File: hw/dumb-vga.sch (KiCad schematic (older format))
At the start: 21 parts, among them IC1 74HC590N, IC2 74HC590N, IC3 74HC590N, IC4 74HC574N, P1 CONN_01X02, U1 A29040C, X1 VGAF

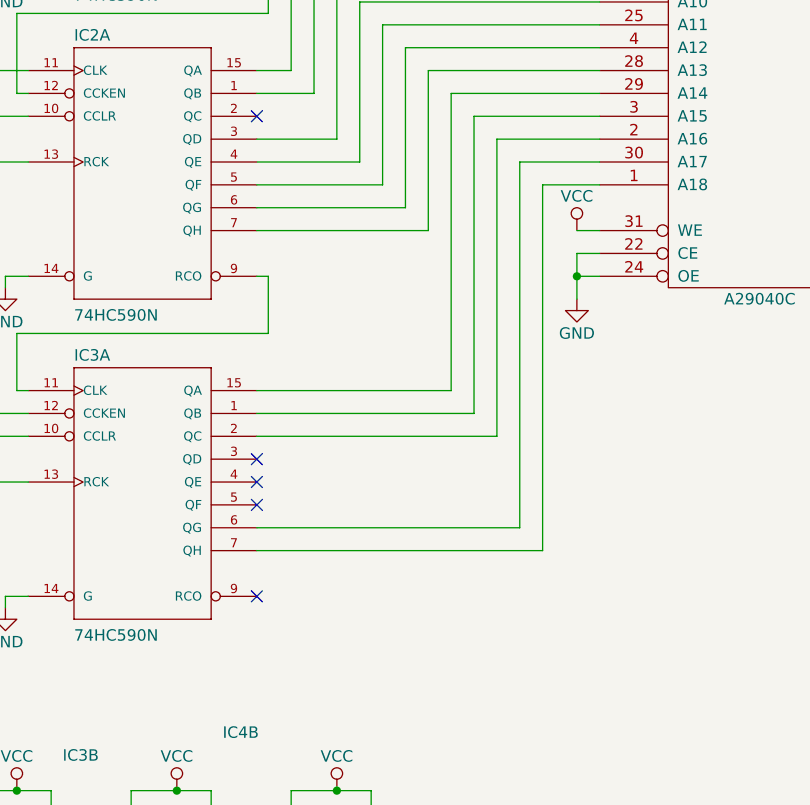
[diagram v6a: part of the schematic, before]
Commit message: Add control over animation rate
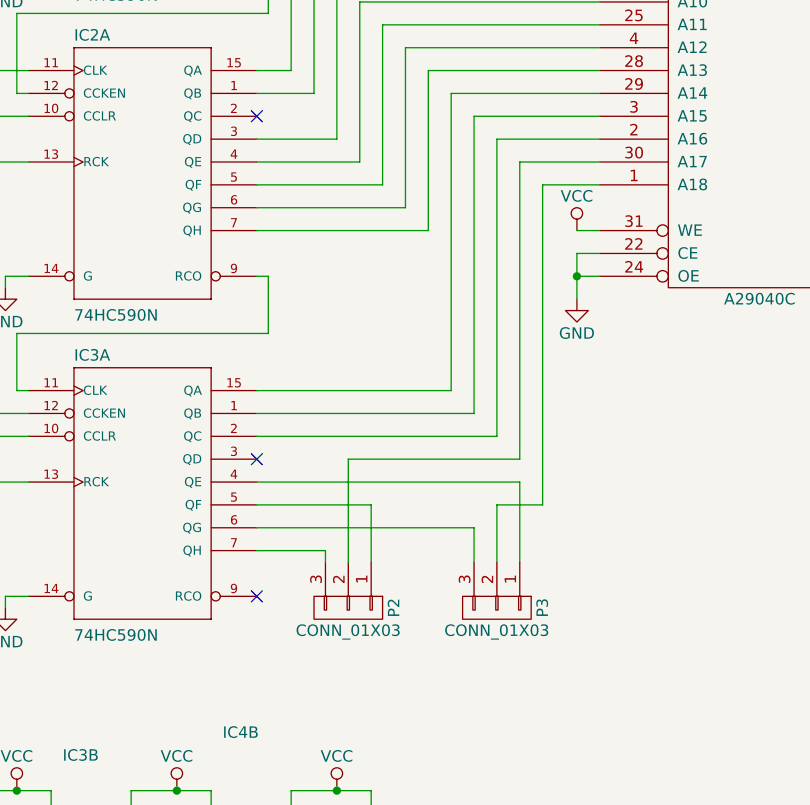
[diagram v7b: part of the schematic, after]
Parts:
- added P2, P3: CONN_01X03, symbol CONN_01X03
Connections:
- net at IC3.4 (QE): now also P3.1 (P1)
- net at IC3.5 (QF): now also P2.1 (P1)
- net at IC3.6 (QG): now also P3.3 (P3); no longer U1.30 (A17)
- net at IC3.7 (QH): now also P2.3 (P3); no longer U1.1 (A18)
- new net: P3.2 (P2), U1.1 (A18)
- new net: P2.2 (P2), U1.30 (A17)
- no-connect marks 14 -> 12
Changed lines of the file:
@@
 Title "Dumb VGA"
 Date ""
-Rev "v0.5"
+Rev "v0.6"
 Comp ""
 Comment1 "Simple circuit to generate VGA-like signal"
@@
 $EndComp
 $Comp
-L VCC #PWR01
+L VCC #PWR11
 U 1 1 56DA1B02
 P 2150 5950
-F 0 "#PWR01" H 2150 5800 50  0001 C CNN
+F 0 "#PWR11" H 2150 5800 50  0001 C CNN
 F 1 "VCC" H 2150 6100 50  0000 C CNN
 F 2 "" H 2150 5950 50  0000 C CNN
@@
 $EndComp
 $Comp
-L VCC #PWR02
+L VCC #PWR21
 U 1 1 56DA1B3E
 P 2850 5950
-F 0 "#PWR02" H 2850 5800 50  0001 C CNN
+F 0 "#PWR21" H 2850 5800 50  0001 C CNN
 F 1 "VCC" H 2850 6100 50  0000 C CNN
 F 2 "" H 2850 5950 50  0000 C CNN
@@
 $EndComp
 $Comp
-L VCC #PWR03
+L VCC #PWR23
 U 1 1 56DA1B5E
 P 3550 5950
-F 0 "#PWR03" H 3550 5800 50  0001 C CNN
+F 0 "#PWR23" H 3550 5800 50  0001 C CNN
 F 1 "VCC" H 3550 6100 50  0000 C CNN
 F 2 "" H 3550 5950 50  0000 C CNN
@@
 $EndComp
 $Comp
-L GND #PWR04
+L GND #PWR24
 U 1 1 56DA1EF3
 P 3550 6750
-F 0 "#PWR04" H 3550 6500 50  0001 C CNN
+F 0 "#PWR24" H 3550 6500 50  0001 C CNN
 F 1 "GND" H 3550 6600 50  0000 C CNN
 F 2 "" H 3550 6750 50  0000 C CNN
@@
 $EndComp
 $Comp
-L GND #PWR05
+L GND #PWR22
 U 1 1 56DA1FE2
 P 2850 6750
-F 0 "#PWR05" H 2850 6500 50  0001 C CNN
+F 0 "#PWR22" H 2850 6500 50  0001 C CNN
 F 1 "GND" H 2850 6600 50  0000 C CNN
 F 2 "" H 2850 6750 50  0000 C CNN
@@
 $EndComp
 $Comp
-L GND #PWR06
+L GND #PWR12
 U 1 1 56DA2011
 P 2150 6750
-F 0 "#PWR06" H 2150 6500 50  0001 C CNN
+F 0 "#PWR12" H 2150 6500 50  0001 C CNN
 F 1 "GND" H 2150 6600 50  0000 C CNN
 F 2 "" H 2150 6750 50  0000 C CNN
@@
 $EndComp
 NoConn ~ 3900 5100
-NoConn ~ 3900 4500
-NoConn ~ 3900 4600
-NoConn ~ 3900 4700
 $Comp
 L XO-8 QG1
@@
 $EndComp
 $Comp
-L VCC #PWR07
+L VCC #PWR3
 U 1 1 56DA29D7
 P 950 1100
-F 0 "#PWR07" H 950 950 50  0001 C CNN
+F 0 "#PWR3" H 950 950 50  0001 C CNN
 F 1 "VCC" H 950 1250 50  0000 C CNN
 F 2 "" H 950 1100 50  0000 C CNN
@@
 $EndComp
 $Comp
-L GND #PWR08
+L GND #PWR4
 U 1 1 56DA2A09
 P 950 1700
-F 0 "#PWR08" H 950 1450 50  0001 C CNN
+F 0 "#PWR4" H 950 1450 50  0001 C CNN
 F 1 "GND" H 950 1550 50  0000 C CNN
 F 2 "" H 950 1700 50  0000 C CNN
@@
 NoConn ~ 2050 1200
 $Comp
-L GND #PWR09
+L GND #PWR28
 U 1 1 56DA2E52
 P 5300 3800
-F 0 "#PWR09" H 5300 3550 50  0001 C CNN
+F 0 "#PWR28" H 5300 3550 50  0001 C CNN
 F 1 "GND" H 5300 3650 50  0000 C CNN
 F 2 "" H 5300 3800 50  0000 C CNN
@@
 $EndComp
 $Comp
-L VCC #PWR010
+L VCC #PWR27
 U 1 1 56DA2FBD
 P 5300 3500
-F 0 "#PWR010" H 5300 3350 50  0001 C CNN
+F 0 "#PWR27" H 5300 3350 50  0001 C CNN
 F 1 "VCC" H 5300 3650 50  0000 C CNN
 F 2 "" H 5300 3500 50  0000 C CNN
@@
 $EndComp
 $Comp
-L GND #PWR011
+L GND #PWR18
 U 1 1 56DA30CB
 P 2800 2350
-F 0 "#PWR011" H 2800 2100 50  0001 C CNN
+F 0 "#PWR18" H 2800 2100 50  0001 C CNN
 F 1 "GND" H 2800 2200 50  0000 C CNN
 F 2 "" H 2800 2350 50  0000 C CNN
@@
 $EndComp
 $Comp
-L GND #PWR012
+L GND #PWR19
 U 1 1 56DA30FD
 P 2800 3750
-F 0 "#PWR012" H 2800 3500 50  0001 C CNN
+F 0 "#PWR19" H 2800 3500 50  0001 C CNN
 F 1 "GND" H 2800 3600 50  0000 C CNN
 F 2 "" H 2800 3750 50  0000 C CNN
@@
 $EndComp
 $Comp
-L GND #PWR013
+L GND #PWR20
 U 1 1 56DA31B1
 P 2800 5150
-F 0 "#PWR013" H 2800 4900 50  0001 C CNN
+F 0 "#PWR20" H 2800 4900 50  0001 C CNN
 F 1 "GND" H 2800 5000 50  0000 C CNN
 F 2 "" H 2800 5150 50  0000 C CNN
@@
 $EndComp
 $Comp
-L GND #PWR014
+L GND #PWR16
 U 1 1 56DA3E4A
 P 2500 1700
-F 0 "#PWR014" H 2500 1450 50  0001 C CNN
+F 0 "#PWR16" H 2500 1450 50  0001 C CNN
 F 1 "GND" H 2500 1550 50  0000 C CNN
 F 2 "" H 2500 1700 50  0000 C CNN
@@
 $EndComp
 $Comp
-L GND #PWR015
+L GND #PWR17
 U 1 1 56DA3EAE
 P 2500 4500
-F 0 "#PWR015" H 2500 4250 50  0001 C CNN
+F 0 "#PWR17" H 2500 4250 50  0001 C CNN
 F 1 "GND" H 2500 4350 50  0000 C CNN
 F 2 "" H 2500 4500 50  0000 C CNN
@@
 $EndComp
 $Comp
-L VCC #PWR016
+L VCC #PWR13
 U 1 1 56DA4042
 P 2350 1600
-F 0 "#PWR016" H 2350 1450 50  0001 C CNN
+F 0 "#PWR13" H 2350 1450 50  0001 C CNN
 F 1 "VCC" H 2350 1750 50  0000 C CNN
 F 2 "" H 2350 1600 50  0000 C CNN
@@
 $EndComp
 $Comp
-L VCC #PWR017
+L VCC #PWR14
 U 1 1 56DA4074
 P 2350 3000
-F 0 "#PWR017" H 2350 2850 50  0001 C CNN
+F 0 "#PWR14" H 2350 2850 50  0001 C CNN
 F 1 "VCC" H 2350 3150 50  0000 C CNN
 F 2 "" H 2350 3000 50  0000 C CNN
@@
 $EndComp
 $Comp
-L VCC #PWR018
+L VCC #PWR15
 U 1 1 56DA40E7
 P 2350 4400
-F 0 "#PWR018" H 2350 4250 50  0001 C CNN
+F 0 "#PWR15" H 2350 4250 50  0001 C CNN
 F 1 "VCC" H 2350 4550 50  0000 C CNN
 F 2 "" H 2350 4400 50  0000 C CNN
@@
 $EndComp
 $Comp
-L VCC #PWR019
+L VCC #PWR9
 U 1 1 56DA442B
 P 1400 5950
-F 0 "#PWR019" H 1400 5800 50  0001 C CNN
+F 0 "#PWR9" H 1400 5800 50  0001 C CNN
 F 1 "VCC" H 1400 6100 50  0000 C CNN
 F 2 "" H 1400 5950 50  0000 C CNN
@@
 $EndComp
 $Comp
-L GND #PWR020
+L GND #PWR10
 U 1 1 56DA445D
 P 1400 6750
-F 0 "#PWR020" H 1400 6500 50  0001 C CNN
+F 0 "#PWR10" H 1400 6500 50  0001 C CNN
 F 1 "GND" H 1400 6600 50  0000 C CNN
 F 2 "" H 1400 6750 50  0000 C CNN
@@
 $EndComp
 $Comp
-L GND #PWR021
+L GND #PWR30
 U 1 1 56DA4B82
 P 9350 2450
-F 0 "#PWR021" H 9350 2200 50  0001 C CNN
+F 0 "#PWR30" H 9350 2200 50  0001 C CNN
 F 1 "GND" H 9350 2300 50  0000 C CNN
 F 2 "" H 9350 2450 50  0000 C CNN
@@
 	8550 2800 8550 2200
 $Comp
-L PWR_FLAG #FLG022
+L PWR_FLAG #FLG1
 U 1 1 56DA6820
 P 850 6050
-F 0 "#FLG022" H 850 6145 50  0001 C CNN
+F 0 "#FLG1" H 850 6145 50  0001 C CNN
 F 1 "PWR_FLAG" H 850 6230 50  0000 C CNN
 F 2 "" H 850 6050 50  0000 C CNN
@@
 $EndComp
 $Comp
-L VCC #PWR023
+L VCC #PWR1
 U 1 1 56DA68DE
 P 850 5950
-F 0 "#PWR023" H 850 5800 50  0001 C CNN
+F 0 "#PWR1" H 850 5800 50  0001 C CNN
 F 1 "VCC" H 850 6100 50  0000 C CNN
 F 2 "" H 850 5950 50  0000 C CNN
@@
 	850  5950 850  6050
 $Comp
-L GND #PWR024
+L GND #PWR2
 U 1 1 56DA6AC0
 P 850 6750
-F 0 "#PWR024" H 850 6500 50  0001 C CNN
+F 0 "#PWR2" H 850 6500 50  0001 C CNN
 F 1 "GND" H 850 6600 50  0000 C CNN
 F 2 "" H 850 6750 50  0000 C CNN
@@
 $EndComp
 $Comp
-L PWR_FLAG #FLG025
+L PWR_FLAG #FLG2
 U 1 1 56DA6B84
 P 850 6650
-F 0 "#FLG025" H 850 6745 50  0001 C CNN
+F 0 "#FLG2" H 850 6745 50  0001 C CNN
 F 1 "PWR_FLAG" H 850 6830 50  0000 C CNN
 F 2 "" H 850 6650 50  0000 C CNN
@@
 	8550 2200 8100 2200
 $Comp
-L GND #PWR026
+L GND #PWR29
 U 1 1 56DACC69
 P 7000 2600
-F 0 "#PWR026" H 7000 2350 50  0001 C CNN
+F 0 "#PWR29" H 7000 2350 50  0001 C CNN
 F 1 "GND" H 7000 2450 50  0000 C CNN
 F 2 "" H 7000 2600 50  0000 C CNN
@@
 $EndComp
 $Comp
-L VCC #PWR027
+L VCC #PWR25
 U 1 1 56DAD35F
 P 4250 5950
-F 0 "#PWR027" H 4250 5800 50  0001 C CNN
+F 0 "#PWR25" H 4250 5800 50  0001 C CNN
 F 1 "VCC" H 4250 6100 50  0000 C CNN
 F 2 "" H 4250 5950 50  0000 C CNN
@@
 $EndComp
 $Comp
-L GND #PWR028
+L GND #PWR26
 U 1 1 56DAD3AF
 P 4250 6750
-F 0 "#PWR028" H 4250 6500 50  0001 C CNN
+F 0 "#PWR26" H 4250 6500 50  0001 C CNN
 F 1 "GND" H 4250 6600 50  0000 C CNN
 F 2 "" H 4250 6750 50  0000 C CNN
@@
 Connection ~ 4250 5950
 Wire Wire Line
-	3900 4900 5150 4900
-Wire Wire Line
 	5400 3600 5300 3600
 Wire Wire Line
 	5400 3700 5300 3700
 Wire Wire Line
-	5050 3200 5050 4800
-Wire Wire Line
 	5050 3200 5400 3200
 Wire Wire Line
 	5400 3300 5150 3300
-Wire Wire Line
-	5150 3300 5150 4900
 Wire Wire Line
 	7000 2500 7000 2600
@@
 Wire Wire Line
 	4950 4400 3900 4400
-Wire Wire Line
-	5050 4800 3900 4800
 $Comp
 L XO-14 QG2
@@
 Connection ~ 2200 1400
 $Comp
-L VCC #PWR029
+L VCC #PWR5
 U 1 1 56E0A7F2
 P 950 2100
-F 0 "#PWR029" H 950 1950 50  0001 C CNN
+F 0 "#PWR5" H 950 1950 50  0001 C CNN
 F 1 "VCC" H 950 2250 50  0000 C CNN
 F 2 "" H 950 2100 50  0000 C CNN
@@
 $EndComp
 $Comp
-L GND #PWR030
+L GND #PWR6
 U 1 1 56E0A845
 P 950 2700
-F 0 "#PWR030" H 950 2450 50  0001 C CNN
+F 0 "#PWR6" H 950 2450 50  0001 C CNN
 F 1 "GND" H 950 2550 50  0000 C CNN
 F 2 "" H 950 2700 50  0000 C CNN
@@
 $EndComp
 $Comp
-L VCC #PWR031
+L VCC #PWR7
 U 1 1 56E0AC4F
 P 1350 3300
-F 0 "#PWR031" H 1350 3150 50  0001 C CNN
+F 0 "#PWR7" H 1350 3150 50  0001 C CNN
 F 1 "VCC" H 1350 3450 50  0000 C CNN
 F 2 "" H 1350 3300 50  0000 C CNN
@@
 $EndComp
 $Comp
-L GND #PWR032
+L GND #PWR8
 U 1 1 56E0ACA5
 P 1350 3600
-F 0 "#PWR032" H 1350 3350 50  0001 C CNN
+F 0 "#PWR8" H 1350 3350 50  0001 C CNN
 F 1 "GND" H 1350 3450 50  0000 C CNN
 F 2 "" H 1350 3600 50  0000 C CNN
@@
 Wire Wire Line
 	1350 3500 1350 3600
+$Comp
+L CONN_01X03 P3
+U 1 1 56E873E0
+P 4950 5150
+F 0 "P3" H 4950 5350 50  0000 C CNN
+F 1 "CONN_01X03" V 5050 5150 50  0000 C CNN
+F 2 "" H 4950 5150 50  0000 C CNN
+F 3 "" H 4950 5150 50  0000 C CNN
+	1    4950 5150
+	0    1    1    0
+$EndComp
+$Comp
+L CONN_01X03 P2
+U 1 1 56E87448
+P 4300 5150
+F 0 "P2" H 4300 5350 50  0000 C CNN
+F 1 "CONN_01X03" V 4400 5150 50  0000 C CNN
+F 2 "" H 4300 5150 50  0000 C CNN
+F 3 "" H 4300 5150 50  0000 C CNN
+	1    4300 5150
+	0    1    1    0
+$EndComp
+Wire Wire Line
+	3900 4900 4200 4900
+Wire Wire Line
+	4200 4900 4200 4950
+Wire Wire Line
+	3900 4700 4400 4700
+Wire Wire Line
+	4400 4700 4400 4950
+Wire Wire Line
+	3900 4600 5050 4600
+Wire Wire Line
+	5050 4600 5050 4950
+Wire Wire Line
+	3900 4800 4850 4800
+Wire Wire Line
+	4850 4800 4850 4950
+Wire Wire Line
+	4300 4950 4300 4500
+Wire Wire Line
+	4300 4500 5050 4500
+Wire Wire Line
+	5050 4500 5050 3200
+Wire Wire Line
+	4950 4950 4950 4700
+Wire Wire Line
+	4950 4700 5150 4700
+Wire Wire Line
+	5150 4700 5150 3300
+NoConn ~ 3900 4500
 $EndSCHEMATC

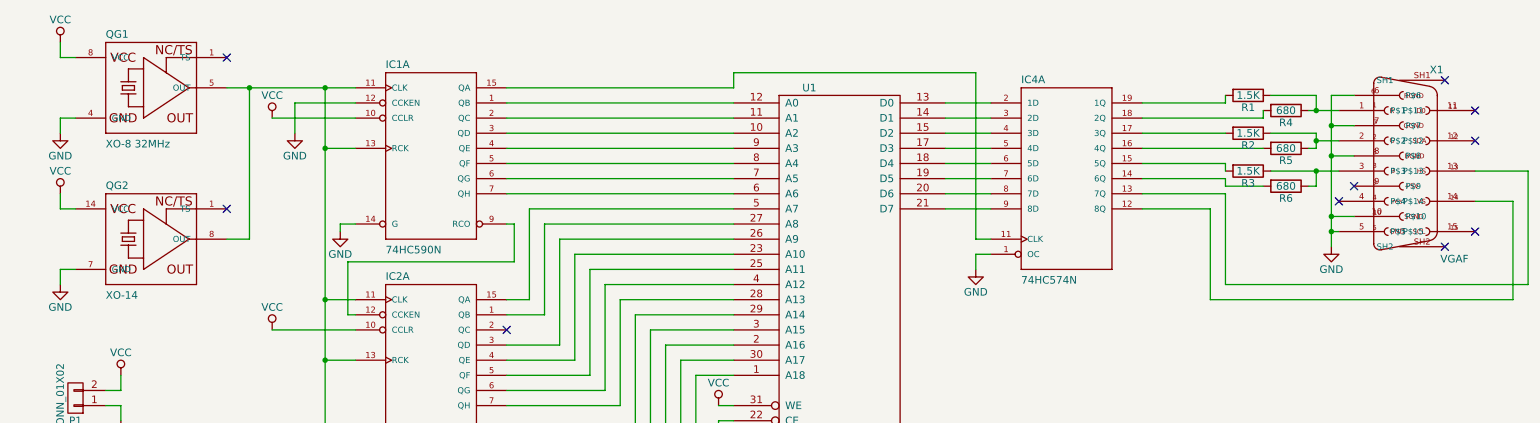
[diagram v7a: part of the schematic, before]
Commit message: Make animation rate switchable
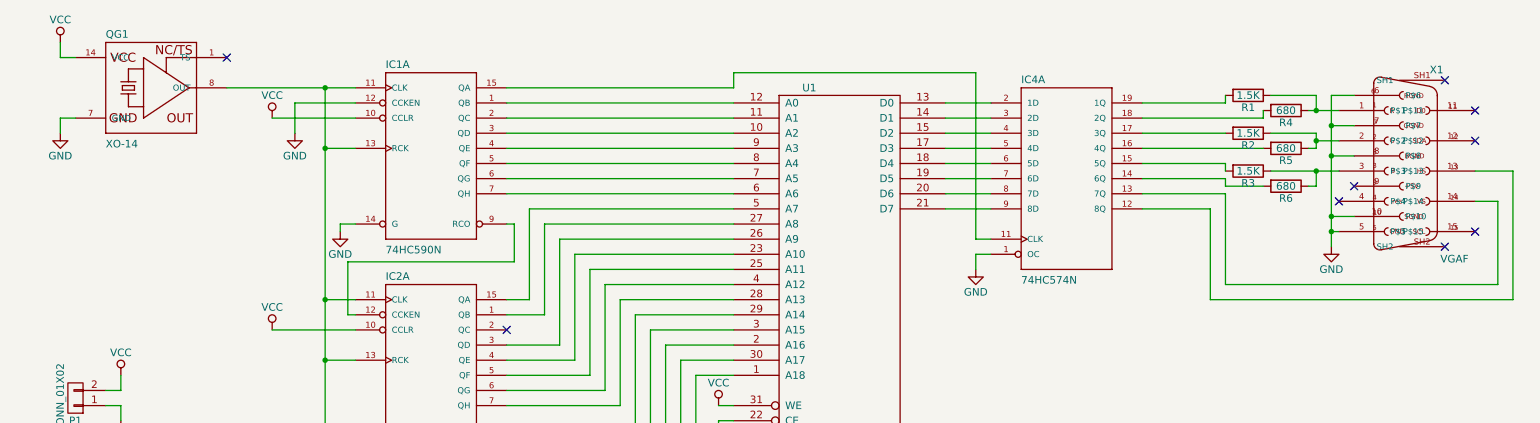
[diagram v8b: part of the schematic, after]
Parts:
- removed QG1: XO-8 32MHz, Housings_DIP:DIP-8_W7.62mm, symbol XO-8
- P2, P3: footprint (none) -> Pin_Headers:Pin_Header_Straight_1x03
- QG1: renamed from QG2; footprint Housings_DIP:DIP-14_W7.62mm -> hw:xo-8-14
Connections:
- net at X1.13 (P$13): now also IC4.12 (8Q); no longer IC4.13 (7Q)
- net at X1.14 (P$14): now also IC4.13 (7Q); no longer IC4.12 (8Q)
- no-connect marks 12 -> 11
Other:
- moved on the sheet: QG1
